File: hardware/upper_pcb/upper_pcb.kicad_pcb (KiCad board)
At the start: 2 copper layers, 54 x 54 mm, 12 parts, among them J5 FPC-6P-0.5mm, SW4 Kailh-GM8.0, SW5 Kailh-GM8.0, SW6 Kailh-BlueDot, SW7 Kailh-BlueDot

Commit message: feat: simplify to 2-layer single-sided routing, all traces on F.Cu
- All signal and power traces moved to F.Cu only
- No vias anywhere - eliminates layer-change complexity
- B.Cu = solid GND pour only (add zone fill in KiCad)
- BAT_PLUS routed on F.Cu around south edge to SW1
- J2 battery and J5 FPC connectors both on F.Cu (THT accessible both sides)
- Lower PCB: 88 segments (was 91 with vias/B.Cu traces)
- Upper PCB: 42 segments (was 52 with B.Cu vias)
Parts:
- J5: moved to F.Cu
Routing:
- net GND: track 90.4 -> 53.6 mm, vias 1 -> 0
- net 3V3: track 58.2 -> 39.2 mm, vias 1 -> 0
- net BTN_R: vias 1 -> 0
- net BTN_L: vias 1 -> 0
- net BTN_FW: vias 1 -> 0
- net BTN_BK: vias 1 -> 0
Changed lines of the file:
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@@
   (gr_text "SW6 BACK" (at 78.0000 94.0000 0) (layer "F.SilkS") (effects (font (size 0.8 0.8) (thickness 0.15))))
   (gr_text "SW7 FWD" (at 122.0000 94.0000 0) (layer "F.SilkS") (effects (font (size 0.8 0.8) (thickness 0.15))))
-  (gr_text "J5 FPC-DN" (at 100.0000 112.0000 0) (layer "B.SilkS") (effects (font (size 0.8 0.8) (thickness 0.15))))
+  (gr_text "J5 FPC-DN" (at 100.0000 112.0000 0) (layer "F.SilkS") (effects (font (size 0.8 0.8) (thickness 0.15))))
   (gr_text "UPPER R1.6" (at 100.0000 122.0000 0) (layer "F.SilkS") (effects (font (size 0.8 0.8) (thickness 0.15))))
   (gr_text "FWD" (at 100.0000 76.0000 0) (layer "F.SilkS") (effects (font (size 0.8 0.8) (thickness 0.15))))
@@
       (layers "F.Cu" "F.Mask") (net 6 "BTN_FW"))
   )
-  (footprint "J5" (layer "B.Cu") (at 100.0000 108.0000 0)
-    (fp_text reference "J5" (at 0 -3) (layer "B.SilkS") (effects (font (size 0.8 0.8) (thickness 0.15))))
+  (footprint "J5" (layer "F.Cu") (at 100.0000 108.0000 0)
+    (fp_text reference "J5" (at 0 -3) (layer "F.SilkS") (effects (font (size 0.8 0.8) (thickness 0.15))))
     (fp_text value "FPC-6P-0.5mm" (at 0 3) (layer "F.Fab") hide)
     (pad "1" smd rect (at -1.2500 0.0000) (size 0.4000 1.2000)
-      (layers "B.Cu" "B.Mask") (net 2 "3V3"))
+      (layers "F.Cu" "F.Mask") (net 2 "3V3"))
     (pad "2" smd rect (at -0.7500 0.0000) (size 0.4000 1.2000)
-      (layers "B.Cu" "B.Mask") (net 1 "GND"))
+      (layers "F.Cu" "F.Mask") (net 1 "GND"))
     (pad "3" smd rect (at -0.2500 0.0000) (size 0.4000 1.2000)
-      (layers "B.Cu" "B.Mask") (net 3 "BTN_L"))
+      (layers "F.Cu" "F.Mask") (net 3 "BTN_L"))
     (pad "4" smd rect (at 0.2500 0.0000) (size 0.4000 1.2000)
-      (layers "B.Cu" "B.Mask") (net 4 "BTN_R"))
+      (layers "F.Cu" "F.Mask") (net 4 "BTN_R"))
     (pad "5" smd rect (at 0.7500 0.0000) (size 0.4000 1.2000)
-      (layers "B.Cu" "B.Mask") (net 5 "BTN_BK"))
+      (layers "F.Cu" "F.Mask") (net 5 "BTN_BK"))
     (pad "6" smd rect (at 1.2500 0.0000) (size 0.4000 1.2000)
-      (layers "B.Cu" "B.Mask") (net 6 "BTN_FW"))
+      (layers "F.Cu" "F.Mask") (net 6 "BTN_FW"))
     (pad "7" smd rect (at -2.5000 0.8000) (size 1.2000 1.8000)
-      (layers "B.Cu" "B.Mask") (net 1 "GND"))
+      (layers "F.Cu" "F.Mask") (net 1 "GND"))
     (pad "8" smd rect (at 2.5000 0.8000) (size 1.2000 1.8000)
-      (layers "B.Cu" "B.Mask") (net 1 "GND"))
+      (layers "F.Cu" "F.Mask") (net 1 "GND"))
   )
   (footprint "R1" (layer "F.Cu") (at 89.0000 95.0000 0)
@@
       (drill 2.2000) (layers "*.Cu" "*.Mask") (net 1 "GND"))
   )
-# ===== COPPER TRACES =====
-  (via (at 98.7500 108.0000) (size 0.8000) (drill 0.4000) (layers "F.Cu" "B.Cu") (net 2))
+# ===== COPPER TRACES (F.Cu only) =====
   (segment (start 98.7500 108.0000) (end 98.7500 96.0000) (width 0.3500) (layer "F.Cu") (net 2))
   (segment (start 98.7500 96.0000) (end 122.0000 96.0000) (width 0.3500) (layer "F.Cu") (net 2))
-  (segment (start 98.7500 96.0000) (end 88.5000 96.0000) (width 0.3500) (layer "F.Cu") (net 2))
+  (segment (start 88.5000 96.0000) (end 88.5000 96.0000) (width 0.3500) (layer "F.Cu") (net 2))
   (segment (start 88.5000 96.0000) (end 88.5000 95.0000) (width 0.3500) (layer "F.Cu") (net 2))
-  (segment (start 108.0000 96.0000) (end 108.5000 96.0000) (width 0.3500) (layer "F.Cu") (net 2))
+  (segment (start 108.5000 96.0000) (end 108.5000 96.0000) (width 0.3500) (layer "F.Cu") (net 2))
   (segment (start 108.5000 96.0000) (end 108.5000 95.0000) (width 0.3500) (layer "F.Cu") (net 2))
   (segment (start 80.0000 96.0000) (end 81.5000 96.0000) (width 0.3500) (layer "F.Cu") (net 2))
@@
   (segment (start 118.0000 96.0000) (end 117.5000 96.0000) (width 0.3500) (layer "F.Cu") (net 2))
   (segment (start 117.5000 96.0000) (end 117.5000 96.0000) (width 0.3500) (layer "F.Cu") (net 2))
-  (via (at 99.2500 108.0000) (size 0.8000) (drill 0.4000) (layers "F.Cu" "B.Cu") (net 1))
   (segment (start 99.2500 108.0000) (end 99.2500 98.0000) (width 0.3500) (layer "F.Cu") (net 1))
   (segment (start 99.2500 98.0000) (end 122.0000 98.0000) (width 0.3500) (layer "F.Cu") (net 1))
-  (segment (start 99.2500 98.0000) (end 90.0000 98.0000) (width 0.3500) (layer "F.Cu") (net 1))
-  (segment (start 90.0000 98.0000) (end 90.0000 91.8100) (width 0.3500) (layer "F.Cu") (net 1))
-  (segment (start 110.0000 98.0000) (end 110.0000 98.0000) (width 0.3500) (layer "F.Cu") (net 1))
-  (segment (start 110.0000 98.0000) (end 110.0000 91.8100) (width 0.3500) (layer "F.Cu") (net 1))
-  (segment (start 80.0000 98.0000) (end 75.5000 98.0000) (width 0.3500) (layer "F.Cu") (net 1))
-  (segment (start 75.5000 98.0000) (end 75.5000 100.0000) (width 0.3500) (layer "F.Cu") (net 1))
-  (segment (start 119.5000 98.0000) (end 119.5000 98.0000) (width 0.3500) (layer "F.Cu") (net 1))
-  (segment (start 119.5000 98.0000) (end 119.5000 100.0000) (width 0.3500) (layer "F.Cu") (net 1))
-  (segment (start 100.5000 116.0000) (end 110.0000 116.0000) (width 0.3500) (layer "F.Cu") (net 1))
-  (segment (start 110.0000 116.0000) (end 110.0000 98.0000) (width 0.3500) (layer "F.Cu") (net 1))
-  (via (at 99.7500 108.0000) (size 0.8000) (drill 0.4000) (layers "F.Cu" "B.Cu") (net 3))
+  (segment (start 90.0000 91.8100) (end 90.0000 91.8100) (width 0.3500) (layer "F.Cu") (net 1))
+  (segment (start 90.0000 91.8100) (end 90.0000 98.0000) (width 0.3500) (layer "F.Cu") (net 1))
+  (segment (start 110.0000 91.8100) (end 110.0000 91.8100) (width 0.3500) (layer "F.Cu") (net 1))
+  (segment (start 110.0000 91.8100) (end 110.0000 98.0000) (width 0.3500) (layer "F.Cu") (net 1))
+  (segment (start 75.5000 100.0000) (end 80.0000 100.0000) (width 0.3500) (layer "F.Cu") (net 1))
+  (segment (start 80.0000 100.0000) (end 80.0000 98.0000) (width 0.3500) (layer "F.Cu") (net 1))
+  (segment (start 119.5000 100.0000) (end 119.5000 100.0000) (width 0.3500) (layer "F.Cu") (net 1))
+  (segment (start 119.5000 100.0000) (end 119.5000 98.0000) (width 0.3500) (layer "F.Cu") (net 1))
   (segment (start 99.7500 108.0000) (end 99.7500 104.0000) (width 0.2500) (layer "F.Cu") (net 3))
   (segment (start 99.7500 104.0000) (end 89.5000 104.0000) (width 0.2500) (layer "F.Cu") (net 3))
@@
   (segment (start 89.5000 95.0000) (end 93.8100 95.0000) (width 0.2500) (layer "F.Cu") (net 3))
   (segment (start 93.8100 95.0000) (end 93.8100 88.0000) (width 0.2500) (layer "F.Cu") (net 3))
-  (via (at 100.2500 108.0000) (size 0.8000) (drill 0.4000) (layers "F.Cu" "B.Cu") (net 4))
   (segment (start 100.2500 108.0000) (end 100.2500 105.0000) (width 0.2500) (layer "F.Cu") (net 4))
   (segment (start 100.2500 105.0000) (end 109.5000 105.0000) (width 0.2500) (layer "F.Cu") (net 4))
@@
   (segment (start 109.5000 95.0000) (end 113.8100 95.0000) (width 0.2500) (layer "F.Cu") (net 4))
   (segment (start 113.8100 95.0000) (end 113.8100 88.0000) (width 0.2500) (layer "F.Cu") (net 4))
-  (via (at 100.7500 108.0000) (size 0.8000) (drill 0.4000) (layers "F.Cu" "B.Cu") (net 5))
   (segment (start 100.7500 108.0000) (end 100.7500 102.0000) (width 0.2500) (layer "F.Cu") (net 5))
   (segment (start 100.7500 102.0000) (end 82.0000 102.0000) (width 0.2500) (layer "F.Cu") (net 5))
@@
   (segment (start 82.5000 96.0000) (end 80.5000 96.0000) (width 0.2500) (layer "F.Cu") (net 5))
   (segment (start 80.5000 96.0000) (end 80.5000 100.0000) (width 0.2500) (layer "F.Cu") (net 5))
-  (via (at 101.2500 108.0000) (size 0.8000) (drill 0.4000) (layers "F.Cu" "B.Cu") (net 6))
   (segment (start 101.2500 108.0000) (end 101.2500 103.0000) (width 0.2500) (layer "F.Cu") (net 6))
   (segment (start 101.2500 103.0000) (end 118.0000 103.0000) (width 0.2500) (layer "F.Cu") (net 6))
@@
   (segment (start 118.5000 96.0000) (end 124.5000 96.0000) (width 0.2500) (layer "F.Cu") (net 6))
   (segment (start 124.5000 96.0000) (end 124.5000 100.0000) (width 0.2500) (layer "F.Cu") (net 6))
-  (segment (start 99.5000 116.0000) (end 99.2500 116.0000) (width 0.3500) (layer "F.Cu") (net 2))
-  (segment (start 99.2500 116.0000) (end 99.2500 108.0000) (width 0.3500) (layer "F.Cu") (net 2))
 )

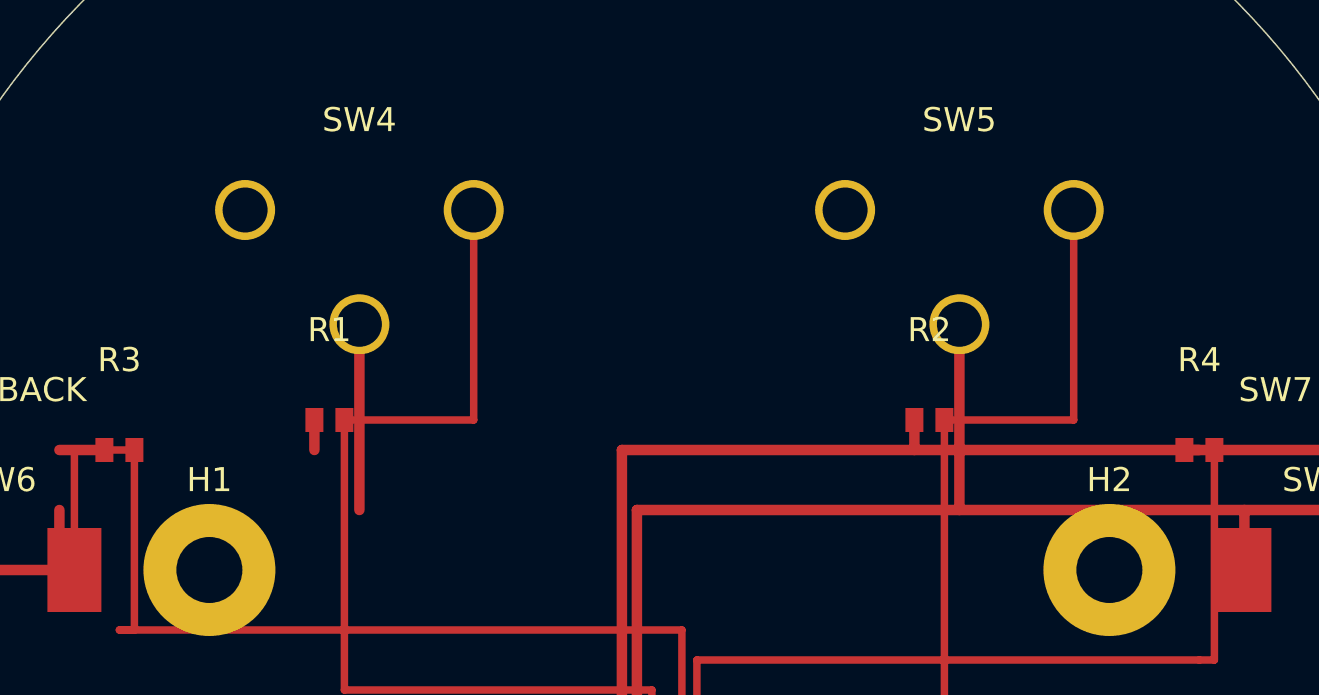
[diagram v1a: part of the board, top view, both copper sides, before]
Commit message: fix: correct SW4/SW5 GM8.0 footprint - 3 pins horizontal, 5.08mm pitch
Previous footprint was wrong (Cherry keyboard MX triangle layout).
Kailh GM 8.0 uses Omron D2FC-F-7N standard footprint:
  NO(-5.08,0) -- COM(0,0) -- NC(+5.08,0)  all on same horizontal axis
  5.08mm (0.2-inch) pin-to-pin pitch
  1.0mm drill, 1.8mm pad diameter

Updated in:
- gen_kicad_pcb.py: gm8_fp() function corrected
- gen_gerbers.py: pad positions + drill holes + silkscreen corrected
- add_traces.py: SW4/SW5 COM and NO trace endpoints corrected
- upper_pcb.kicad_pcb: regenerated with correct footprint
- upper_pcb_gerbers_v1.7.zip: regenerated Gerbers
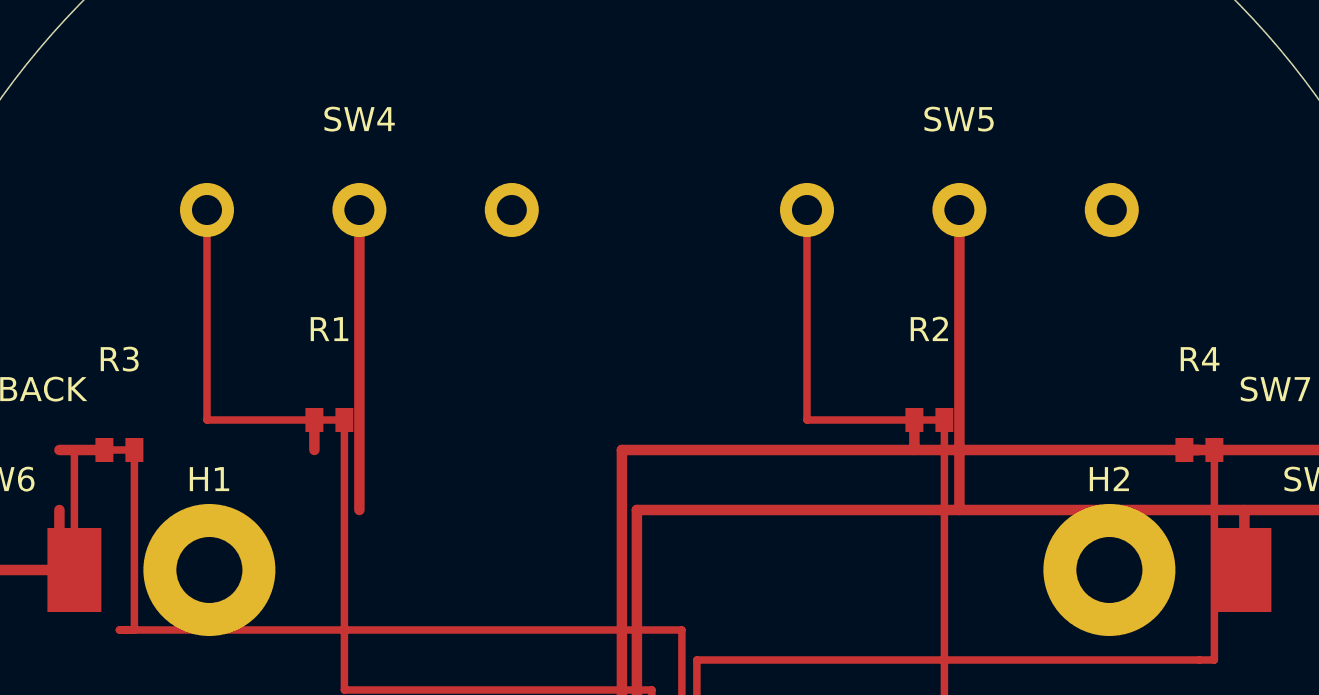
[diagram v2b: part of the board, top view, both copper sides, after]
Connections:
- SW4 pad 1: GND -> BTN_L
- SW4 pad 3: BTN_L -> GND
- SW5 pad 1: GND -> BTN_R
- SW5 pad 3: BTN_R -> GND
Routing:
- net GND: track 53.6 -> 61.2 mm
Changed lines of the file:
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@@
     (fp_text reference "SW4" (at 0 -3) (layer "F.SilkS") (effects (font (size 0.8 0.8) (thickness 0.15))))
     (fp_text value "Kailh-GM8.0" (at 0 3) (layer "F.Fab") hide)
-    (pad "1" thru_hole circle (at -3.8100 0.0000) (size 2.0000 2.0000)
-      (drill 1.5000) (layers "*.Cu" "*.Mask") (net 1 "GND"))
-    (pad "2" thru_hole circle (at 0.0000 3.8100) (size 2.0000 2.0000)
-      (drill 1.5000) (layers "*.Cu" "*.Mask") (net 1 "GND"))
-    (pad "3" thru_hole circle (at 3.8100 0.0000) (size 2.0000 2.0000)
-      (drill 1.5000) (layers "*.Cu" "*.Mask") (net 3 "BTN_L"))
+    (pad "1" thru_hole circle (at -5.0800 0.0000) (size 1.8000 1.8000)
+      (drill 1.0000) (layers "*.Cu" "*.Mask") (net 3 "BTN_L"))
+    (pad "2" thru_hole circle (at 0.0000 0.0000) (size 1.8000 1.8000)
+      (drill 1.0000) (layers "*.Cu" "*.Mask") (net 1 "GND"))
+    (pad "3" thru_hole circle (at 5.0800 0.0000) (size 1.8000 1.8000)
+      (drill 1.0000) (layers "*.Cu" "*.Mask") (net 1 "GND"))
   )
   (footprint "SW5" (layer "F.Cu") (at 110.0000 88.0000 0)
     (fp_text reference "SW5" (at 0 -3) (layer "F.SilkS") (effects (font (size 0.8 0.8) (thickness 0.15))))
     (fp_text value "Kailh-GM8.0" (at 0 3) (layer "F.Fab") hide)
-    (pad "1" thru_hole circle (at -3.8100 0.0000) (size 2.0000 2.0000)
-      (drill 1.5000) (layers "*.Cu" "*.Mask") (net 1 "GND"))
-    (pad "2" thru_hole circle (at 0.0000 3.8100) (size 2.0000 2.0000)
-      (drill 1.5000) (layers "*.Cu" "*.Mask") (net 1 "GND"))
-    (pad "3" thru_hole circle (at 3.8100 0.0000) (size 2.0000 2.0000)
-      (drill 1.5000) (layers "*.Cu" "*.Mask") (net 4 "BTN_R"))
+    (pad "1" thru_hole circle (at -5.0800 0.0000) (size 1.8000 1.8000)
+      (drill 1.0000) (layers "*.Cu" "*.Mask") (net 4 "BTN_R"))
+    (pad "2" thru_hole circle (at 0.0000 0.0000) (size 1.8000 1.8000)
+      (drill 1.0000) (layers "*.Cu" "*.Mask") (net 1 "GND"))
+    (pad "3" thru_hole circle (at 5.0800 0.0000) (size 1.8000 1.8000)
+      (drill 1.0000) (layers "*.Cu" "*.Mask") (net 1 "GND"))
   )
   (footprint "SW6" (layer "F.Cu") (at 78.0000 100.0000 0)
@@
   (segment (start 99.2500 108.0000) (end 99.2500 98.0000) (width 0.3500) (layer "F.Cu") (net 1))
   (segment (start 99.2500 98.0000) (end 122.0000 98.0000) (width 0.3500) (layer "F.Cu") (net 1))
-  (segment (start 90.0000 91.8100) (end 90.0000 91.8100) (width 0.3500) (layer "F.Cu") (net 1))
-  (segment (start 90.0000 91.8100) (end 90.0000 98.0000) (width 0.3500) (layer "F.Cu") (net 1))
-  (segment (start 110.0000 91.8100) (end 110.0000 91.8100) (width 0.3500) (layer "F.Cu") (net 1))
-  (segment (start 110.0000 91.8100) (end 110.0000 98.0000) (width 0.3500) (layer "F.Cu") (net 1))
+  (segment (start 90.0000 88.0000) (end 90.0000 88.0000) (width 0.3500) (layer "F.Cu") (net 1))
+  (segment (start 90.0000 88.0000) (end 90.0000 98.0000) (width 0.3500) (layer "F.Cu") (net 1))
+  (segment (start 110.0000 88.0000) (end 110.0000 88.0000) (width 0.3500) (layer "F.Cu") (net 1))
+  (segment (start 110.0000 88.0000) (end 110.0000 98.0000) (width 0.3500) (layer "F.Cu") (net 1))
   (segment (start 75.5000 100.0000) (end 80.0000 100.0000) (width 0.3500) (layer "F.Cu") (net 1))
   (segment (start 80.0000 100.0000) (end 80.0000 98.0000) (width 0.3500) (layer "F.Cu") (net 1))
@@
   (segment (start 99.7500 104.0000) (end 89.5000 104.0000) (width 0.2500) (layer "F.Cu") (net 3))
   (segment (start 89.5000 104.0000) (end 89.5000 95.0000) (width 0.2500) (layer "F.Cu") (net 3))
-  (segment (start 89.5000 95.0000) (end 93.8100 95.0000) (width 0.2500) (layer "F.Cu") (net 3))
-  (segment (start 93.8100 95.0000) (end 93.8100 88.0000) (width 0.2500) (layer "F.Cu") (net 3))
+  (segment (start 89.5000 95.0000) (end 84.9200 95.0000) (width 0.2500) (layer "F.Cu") (net 3))
+  (segment (start 84.9200 95.0000) (end 84.9200 88.0000) (width 0.2500) (layer "F.Cu") (net 3))
   (segment (start 100.2500 108.0000) (end 100.2500 105.0000) (width 0.2500) (layer "F.Cu") (net 4))
   (segment (start 100.2500 105.0000) (end 109.5000 105.0000) (width 0.2500) (layer "F.Cu") (net 4))
   (segment (start 109.5000 105.0000) (end 109.5000 95.0000) (width 0.2500) (layer "F.Cu") (net 4))
-  (segment (start 109.5000 95.0000) (end 113.8100 95.0000) (width 0.2500) (layer "F.Cu") (net 4))
-  (segment (start 113.8100 95.0000) (end 113.8100 88.0000) (width 0.2500) (layer "F.Cu") (net 4))
+  (segment (start 109.5000 95.0000) (end 104.9200 95.0000) (width 0.2500) (layer "F.Cu") (net 4))
+  (segment (start 104.9200 95.0000) (end 104.9200 88.0000) (width 0.2500) (layer "F.Cu") (net 4))
   (segment (start 100.7500 108.0000) (end 100.7500 102.0000) (width 0.2500) (layer "F.Cu") (net 5))
   (segment (start 100.7500 102.0000) (end 82.0000 102.0000) (width 0.2500) (layer "F.Cu") (net 5))
